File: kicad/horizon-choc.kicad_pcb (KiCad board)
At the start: 2 copper layers, 252.5 x 68 mm, 96 parts, among them J1 OLED, SW1 SW_Push, SW10 SW_Push, SW11 SW_Push, SW12 SW_Push, SW13 SW_Push, SW14 SW_Push, SW15 SW_Push, SW16 SW_Push, SW17 SW_Push, SW18 SW_Push, SW19 SW_Push, SW2 SW_Push, SW20 SW_Push, SW21 SW_Push, SW22 SW_Push, SW23 SW_Push, SW24 SW_Push, SW25 SW_Push, SW26 SW_Push, SW27 SW_Push, SW28 SW_Push, SW29 SW_Push, SW3 SW_Push, SW30 SW_Push, SW31 SW_Push, SW32 SW_Push, SW33 SW_Push, SW34 SW_Push, SW35 SW_Push, SW36 SW_Push, SW37 SW_Push, SW38 SW_Push, SW39 SW_Push, SW4 SW_Push, SW40 SW_Push, SW41 SW_Push, SW42 SW_Push, SW5 SW_Push, SW6 SW_Push, SW7 SW_Push, SW8 SW_Push, SW9 SW_Push, U1 PRO-MICRO

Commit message: Adjust center component layout for MX and Choc consistency.
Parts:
- moved D37 7.50 mm to (192.5, 141.5)
- moved D38 7.50 mm to (194.5, 141.5)
- moved D39 7.50 mm to (196.5, 141.5)
- moved D40 7.50 mm to (207.5, 141.5)
- moved D41 7.50 mm to (209.5, 141.5)
- moved D42 7.50 mm to (211.5, 141.5)
- moved TSW1 0.50 mm to (202.0, 141.5), turned to 90 degrees
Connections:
- D1 pad 1: (no net) -> ROW1
- D1 pad 2: (no net) -> Net-(D1-Pad2)
- D10 pad 1: (no net) -> ROW2
- D10 pad 2: (no net) -> Net-(D10-Pad2)
- D11 pad 1: (no net) -> ROW2
- D11 pad 2: (no net) -> Net-(D11-Pad2)
- D12 pad 1: (no net) -> ROW2
- D12 pad 2: (no net) -> Net-(D12-Pad2)
- D13 pad 1: (no net) -> ROW3
- D13 pad 2: (no net) -> Net-(D13-Pad2)
- D14 pad 1: (no net) -> ROW3
- D14 pad 2: (no net) -> Net-(D14-Pad2)
- D15 pad 1: (no net) -> ROW3
- D15 pad 2: (no net) -> Net-(D15-Pad2)
- D16 pad 1: (no net) -> ROW3
- D16 pad 2: (no net) -> Net-(D16-Pad2)
- D17 pad 1: (no net) -> ROW3
- D17 pad 2: (no net) -> Net-(D17-Pad2)
- D18 pad 1: (no net) -> ROW3
- D18 pad 2: (no net) -> Net-(D18-Pad2)
- D19 pad 1: (no net) -> ROW4
- D19 pad 2: (no net) -> Net-(D19-Pad2)
- D2 pad 1: (no net) -> ROW1
- D2 pad 2: (no net) -> Net-(D2-Pad2)
- D20 pad 1: (no net) -> ROW4
- D20 pad 2: (no net) -> Net-(D20-Pad2)
- D21 pad 1: (no net) -> ROW4
- D21 pad 2: (no net) -> Net-(D21-Pad2)
- D22 pad 1: (no net) -> ROW4
- D22 pad 2: (no net) -> Net-(D22-Pad2)
- D23 pad 1: (no net) -> ROW4
- D23 pad 2: (no net) -> Net-(D23-Pad2)
- D24 pad 1: (no net) -> ROW4
- D24 pad 2: (no net) -> Net-(D24-Pad2)
- D25 pad 1: (no net) -> ROW5
- D25 pad 2: (no net) -> Net-(D25-Pad2)
- D26 pad 1: (no net) -> ROW5
- D26 pad 2: (no net) -> Net-(D26-Pad2)
- D27 pad 1: (no net) -> ROW5
- D27 pad 2: (no net) -> Net-(D27-Pad2)
- D28 pad 1: (no net) -> ROW5
- D28 pad 2: (no net) -> Net-(D28-Pad2)
- D29 pad 1: (no net) -> ROW5
- D29 pad 2: (no net) -> Net-(D29-Pad2)
- D3 pad 1: (no net) -> ROW1
- D3 pad 2: (no net) -> Net-(D3-Pad2)
- D30 pad 1: (no net) -> ROW5
- D30 pad 2: (no net) -> Net-(D30-Pad2)
- D31 pad 1: (no net) -> ROW6
- D31 pad 2: (no net) -> Net-(D31-Pad2)
- D32 pad 1: (no net) -> ROW6
- D32 pad 2: (no net) -> Net-(D32-Pad2)
- D33 pad 1: (no net) -> ROW6
- D33 pad 2: (no net) -> Net-(D33-Pad2)
- D34 pad 1: (no net) -> ROW6
- D34 pad 2: (no net) -> Net-(D34-Pad2)
- D35 pad 1: (no net) -> ROW6
- D35 pad 2: (no net) -> Net-(D35-Pad2)
- D36 pad 1: (no net) -> ROW6
- D36 pad 2: (no net) -> Net-(D36-Pad2)
- D37 pad 1: (no net) -> ROW7
- D37 pad 2: (no net) -> Net-(D37-Pad2)
- D38 pad 1: (no net) -> ROW7
- D38 pad 2: (no net) -> Net-(D38-Pad2)
- D39 pad 1: (no net) -> ROW7
- D39 pad 2: (no net) -> Net-(D39-Pad2)
- D4 pad 1: (no net) -> ROW1
- D4 pad 2: (no net) -> Net-(D4-Pad2)
- D40 pad 1: (no net) -> ROW7
- D40 pad 2: (no net) -> Net-(D40-Pad2)
- D41 pad 1: (no net) -> ROW7
- D41 pad 2: (no net) -> Net-(D41-Pad2)
- D42 pad 1: (no net) -> ROW7
- D42 pad 2: (no net) -> Net-(D42-Pad2)
- D5 pad 1: (no net) -> ROW1
- D5 pad 2: (no net) -> Net-(D5-Pad2)
- D6 pad 1: (no net) -> ROW1
- D6 pad 2: (no net) -> Net-(D6-Pad2)
- D7 pad 1: (no net) -> ROW2
- D7 pad 2: (no net) -> Net-(D7-Pad2)
- D8 pad 1: (no net) -> ROW2
- D8 pad 2: (no net) -> Net-(D8-Pad2)
- D9 pad 1: (no net) -> ROW2
- D9 pad 2: (no net) -> Net-(D9-Pad2)
- H1 pad 1: (no net) -> Net-(H1-Pad1)
- H2 pad 1: (no net) -> Net-(H2-Pad1)
- H3 pad 1: (no net) -> Net-(H3-Pad1)
- H4 pad 1: (no net) -> Net-(H4-Pad1)
- J1 pad 1: (no net) -> GND
- J1 pad 2: (no net) -> VCC
- J1 pad 3: (no net) -> SCL
- J1 pad 4: (no net) -> SDA
- TSW1 pad 1: (no net) -> Net-(TSW1-Pad1)
- TSW1 pad 2: (no net) -> GND
- U1 pad 1: (no net) -> ROW2
- U1 pad 10: (no net) -> COL4
- U1 pad 11: (no net) -> COL5
- U1 pad 12: (no net) -> COL6
- U1 pad 13: (no net) -> ROW7
- U1 pad 14: (no net) -> ROW6
- U1 pad 15: (no net) -> ROW5
- U1 pad 16: (no net) -> ROW3
- U1 pad 17: (no net) -> ROW1
- U1 pad 2: (no net) -> ROW4
- U1 pad 21: (no net) -> VCC
- U1 pad 22: (no net) -> Net-(TSW1-Pad1)
- U1 pad 23: (no net) -> GND
- U1 pad 3: (no net) -> GND
- U1 pad 4: (no net) -> GND
- U1 pad 5: (no net) -> SDA
- U1 pad 6: (no net) -> SCL
- U1 pad 7: (no net) -> COL1
- U1 pad 8: (no net) -> COL2
- U1 pad 9: (no net) -> COL3

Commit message: Route traces on choc version
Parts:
- LOGO1: moved to F.Cu
- moved LOGO1 9.04 mm to (176.1, 174.7), turned to 0 degrees
- turned TSW1 to 0 degrees
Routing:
- net COL2: track 0.00 -> 317.8 mm
- net COL1: track 0.00 -> 317.3 mm
- net COL3: track 0.00 -> 312.2 mm
- net COL4: track 0.00 -> 308.4 mm
- net COL5: track 0.00 -> 306.0 mm
- net COL6: track 0.00 -> 304.9 mm
- net Net-(D12-Pad2): track 0.00 -> 115.5 mm
- net Net-(D36-Pad2): track 0.00 -> 113.4 mm
- net Net-(D24-Pad2): track 0.00 -> 112.4 mm
- net Net-(D1-Pad2): track 0.00 -> 104.4 mm
- net Net-(D25-Pad2): track 0.00 -> 101.9 mm
- net Net-(D13-Pad2): track 0.00 -> 101.0 mm
- net Net-(D35-Pad2): track 0.00 -> 96.5 mm
- net Net-(D11-Pad2): track 0.00 -> 95.9 mm
- net Net-(D23-Pad2): track 0.00 -> 94.5 mm
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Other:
- board size 252.5 x 68 mm -> 252 x 68 mm

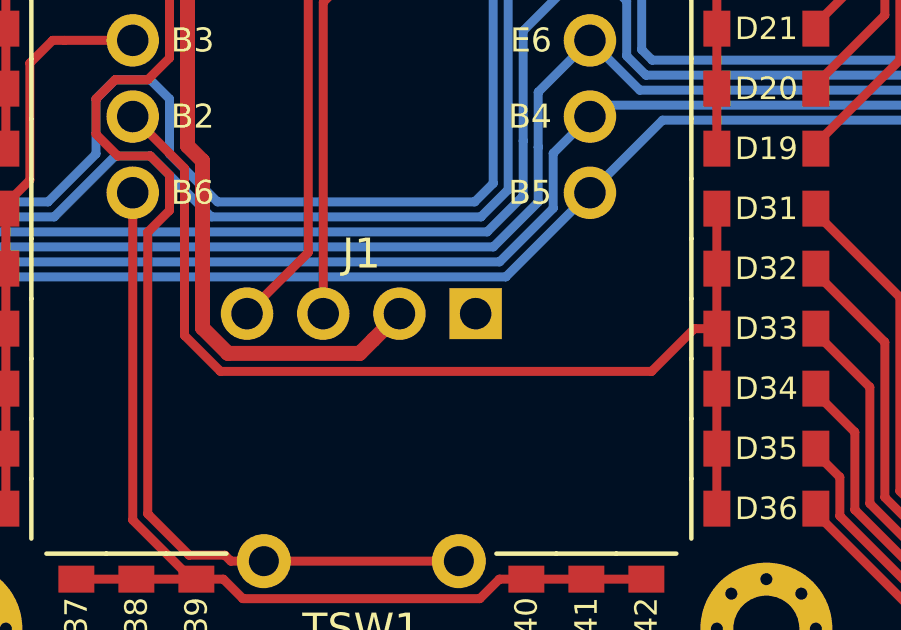
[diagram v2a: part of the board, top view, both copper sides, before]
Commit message: Route Choc board with diodes in center
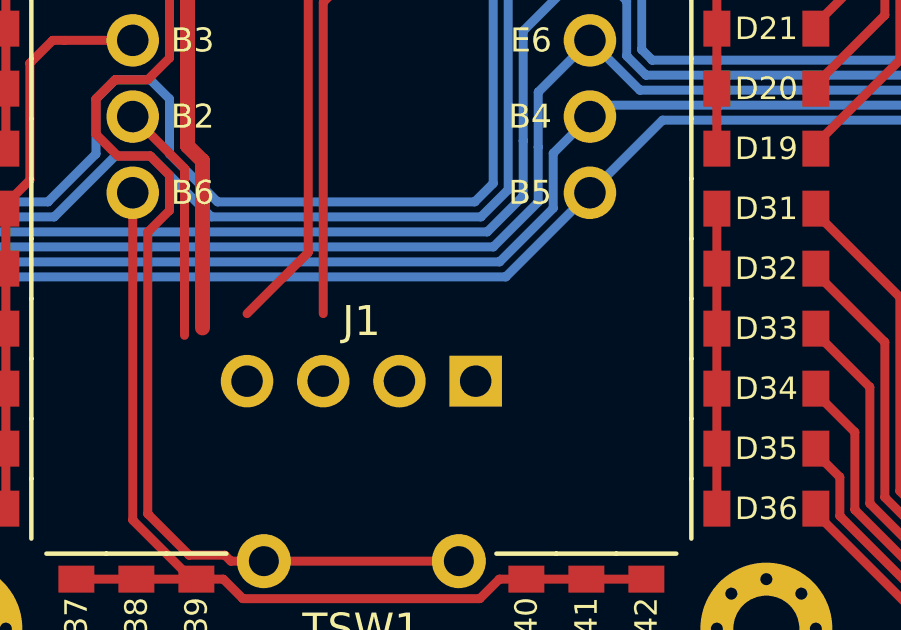
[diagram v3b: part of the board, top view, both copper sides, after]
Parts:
- moved J1 2.25 mm to (202.0, 133.2)
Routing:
- net ROW6: track 36.8 -> 18.0 mm
- net VCC: track 33.3 -> 25.9 mm

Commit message: Use 50 key layout on MX version
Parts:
- removed H5, H6, H7, H8: Hole_Pad, horizon-footprints:Mount_M2
- moved H2 30.0 mm to (245.5, 99.5)
- moved H4 30.0 mm to (245.5, 141.5)
- moved SW10 30.0 mm to (313.0, 103.5)
- moved SW11 30.0 mm to (331.0, 103.5)
- moved SW12 30.0 mm to (349.0, 103.5)
- moved SW19 30.0 mm to (259.0, 120.5)
- moved SW20 30.0 mm to (277.0, 120.5)
- moved SW21 30.0 mm to (295.0, 120.5)
- moved SW22 30.0 mm to (313.0, 120.5)
- moved SW23 30.0 mm to (331.0, 120.5)
- moved SW24 30.0 mm to (349.0, 120.5)
- moved SW31 30.0 mm to (259.0, 137.5)
- moved SW32 30.0 mm to (277.0, 137.5)
- moved SW33 30.0 mm to (295.0, 137.5)
- moved SW34 30.0 mm to (313.0, 137.5)
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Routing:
- net COL2: track 317.8 -> 0.00 mm
- net COL1: track 317.3 -> 0.00 mm
- net COL3: track 312.2 -> 0.00 mm
- net COL4: track 308.4 -> 0.00 mm
- net COL5: track 306.0 -> 0.00 mm
- net COL6: track 304.9 -> 0.00 mm
- net Net-(D12-Pad2): track 115.5 -> 0.00 mm
- net Net-(D36-Pad2): track 113.4 -> 0.00 mm
- net Net-(D24-Pad2): track 112.4 -> 0.00 mm
- net Net-(D1-Pad2): track 104.4 -> 0.00 mm
- net Net-(D25-Pad2): track 101.9 -> 0.00 mm
- net Net-(D13-Pad2): track 101.0 -> 0.00 mm
- net Net-(D35-Pad2): track 96.5 -> 0.00 mm
- net Net-(D11-Pad2): track 95.9 -> 0.00 mm
- net Net-(D23-Pad2): track 94.5 -> 0.00 mm
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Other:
- board size 252 x 68 mm -> 282 x 86.8 mm

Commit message: Implement battery on Choc version, plus bottom and top PCBs
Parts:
- removed the D25 at (202.5, 136.5)
- removed the D39 at (202.5, 142.5)
- removed J1: OLED, horizon-footprints:Header_1x04_2.54mm
- removed the SW25 at (85.0, 137.5)
- removed the SW39 at (204.0, 170.2)
- added D19: D, horizon-footprints:D_SOD-123, F.Cu at (229.0, 125.2)
- added D43: D, horizon-footprints:D_SOD-123, F.Cu at (157.0, 159.2)
- added D44: D, horizon-footprints:D_SOD-123, F.Cu at (175.0, 159.2)
- added D45: D, horizon-footprints:D_SOD-123, F.Cu at (193.0, 159.2)
- added D46: D, horizon-footprints:D_SOD-123, F.Cu at (211.0, 159.2)
- added D47: D, horizon-footprints:D_SOD-123, F.Cu at (229.0, 159.2)
- added D48: D, horizon-footprints:D_SOD-123, F.Cu at (247.0, 159.2)
- added D49: D, horizon-footprints:D_SOD-123, F.Cu at (265.0, 159.2)
- added D50: D, horizon-footprints:D_SOD-123, F.Cu at (283.0, 159.2)
- added D51: D, horizon-footprints:D_SOD-123, F.Cu at (301.0, 159.2)
- added D52: D, horizon-footprints:D_SOD-123, F.Cu at (319.0, 159.2)
- added D7: D, horizon-footprints:D_SOD-123, F.Cu at (229.0, 108.2)
- added H10: Hole_Pad, horizon-footprints:Mount_M2, F.Cu at (215.5, 99.5)
- added H11: Hole_Pad, horizon-footprints:Mount_M2, F.Cu at (188.5, 124.5)
- added H12: Hole_Pad, horizon-footprints:Mount_M2, F.Cu at (215.5, 124.5)
- added H5: Hole_Pad, horizon-footprints:Mount_M2, F.Cu at (94.0, 146.0)
- added H6: Hole_Pad, horizon-footprints:Mount_M2, F.Cu at (166.0, 146.0)
- added H7: Hole_Pad, horizon-footprints:Mount_M2, F.Cu at (238.0, 146.0)
- added H8: Hole_Pad, horizon-footprints:Mount_M2, F.Cu at (310.0, 146.0)
- added H9: Hole_Pad, horizon-footprints:Mount_M2, F.Cu at (188.5, 99.5)
- added SS1: POWER, horizon-footprints:SS12D00, F.Cu at (188.5, 112.0)
- added SW19: SW_Push, horizon-footprints:SW_Choc, F.Cu at (229.0, 120.5)
- added SW43: SW_Push, horizon-footprints:SW_Choc, F.Cu at (157.0, 154.5)
- added SW44: SW_Push, horizon-footprints:SW_Choc, F.Cu at (175.0, 154.5)
- added SW45: SW_Push, horizon-footprints:SW_Choc, F.Cu at (193.0, 154.5)
- added SW46: SW_Push, horizon-footprints:SW_Choc, F.Cu at (211.0, 154.5)
- added SW47: SW_Push, horizon-footprints:SW_Choc, F.Cu at (229.0, 154.5)
- added SW48: SW_Push, horizon-footprints:SW_Choc, F.Cu at (247.0, 154.5)
- added SW49: SW_Push, horizon-footprints:SW_Choc, F.Cu at (265.0, 154.5)
- added SW50: SW_Push, horizon-footprints:SW_Choc, F.Cu at (283.0, 154.5)
- added SW51: SW_Push, horizon-footprints:SW_Choc, F.Cu at (301.0, 154.5)
- added SW52: SW_Push, horizon-footprints:SW_Choc, F.Cu at (319.0, 154.5)
- added SW7: SW_Push, horizon-footprints:SW_Choc, F.Cu at (229.0, 103.5)
- added W1: BATTERY, horizon-footprints:Battery_Wire_Pads, F.Cu at (188.5, 106.2)
- LOGO1: moved to B.Cu
- moved SW39 177.3 mm to (85.0, 154.5)
- moved SW13 174.8 mm to (85.0, 120.5)
- moved D39 153.1 mm to (85.0, 159.2)
- moved D13 150.8 mm to (85.0, 125.2)
- moved SW37 136.1 mm to (301.0, 137.5)
- moved SW38 134.1 mm to (319.0, 137.5), turned to 0 degrees
- moved D40 132.1 mm to (103.0, 159.2)
- moved SW42 129.0 mm to (139.0, 154.5)
- moved SW40 128.0 mm to (103.0, 154.5), turned to 0 degrees
- moved SW41 126.5 mm to (121.0, 154.5), turned to 0 degrees
- moved D25 120.7 mm to (85.0, 142.2), turned to 0 degrees
- moved D1 117.6 mm to (85.0, 108.2), turned to 0 degrees
- moved D38 116.5 mm to (319.0, 142.2), turned to 0 degrees
- moved D41 114.6 mm to (121.0, 159.2)
- moved D14 99.9 mm to (103.0, 125.2), turned to 0 degrees
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- renumbered TSW1 to BTN1, D7 to D13, D13 to D25, D19 to D39, SW7 to SW13, SW13 to SW25, SW19 to SW39
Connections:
- net Net-(TSW1-Pad1) renamed RESET
- D10 pad 1: ROW2 -> ROW1
- D11 pad 1: ROW2 -> ROW1
- D12 pad 1: ROW2 -> ROW1
- D14 pad 1: ROW3 -> ROW2
- D15 pad 1: ROW3 -> ROW2
- D16 pad 1: ROW3 -> ROW2
- D17 pad 1: ROW3 -> ROW2
- D18 pad 1: ROW3 -> ROW2
- D20 pad 1: ROW4 -> ROW2
- D21 pad 1: ROW4 -> ROW2
- D22 pad 1: ROW4 -> ROW2
- D23 pad 1: ROW4 -> ROW2
- D24 pad 1: ROW4 -> ROW2
- D26 pad 1: ROW5 -> ROW3
- D27 pad 1: ROW5 -> ROW3
- D28 pad 1: ROW5 -> ROW3
- D29 pad 1: ROW5 -> ROW3
- D30 pad 1: ROW5 -> ROW3
- D31 pad 1: ROW6 -> ROW3
- D32 pad 1: ROW6 -> ROW3
- D33 pad 1: ROW6 -> ROW3
- D34 pad 1: ROW6 -> ROW3
- D35 pad 1: ROW6 -> ROW3
- D36 pad 1: ROW6 -> ROW3
- D37 pad 1: ROW7 -> ROW3
- D38 pad 1: ROW7 -> ROW3
- D40 pad 1: ROW7 -> ROW4
- D41 pad 1: ROW7 -> ROW4
- D42 pad 1: ROW7 -> ROW4
- D8 pad 1: ROW2 -> ROW1
- D9 pad 1: ROW2 -> ROW1
- SW10 pad 1: COL4 -> COL12
- SW11 pad 1: COL5 -> COL13
- SW12 pad 1: COL6 -> COL14
- SW20 pad 1: COL2 -> COL10
- SW21 pad 1: COL3 -> COL11
- SW22 pad 1: COL4 -> COL12
- SW23 pad 1: COL5 -> COL13
- SW24 pad 1: COL6 -> COL14
- SW31 pad 1: COL1 -> COL7
- SW32 pad 1: COL2 -> COL8
- SW33 pad 1: COL3 -> COL9
- SW34 pad 1: COL4 -> COL10
- SW35 pad 1: COL5 -> COL11
- SW36 pad 1: COL6 -> COL12
- SW37 pad 1: COL1 -> COL13
- SW38 pad 1: COL2 -> COL14
- SW40 pad 1: COL4 -> COL2
- SW41 pad 1: COL5 -> COL3
- SW42 pad 1: COL6 -> COL4
- SW8 pad 1: COL2 -> COL10
- SW9 pad 1: COL3 -> COL11
- U1 pad 1: ROW2 -> ROW1
- U1 pad 10: COL4 -> COL9
- U1 pad 11: COL5 -> COL8
- U1 pad 12: COL6 -> ROW4
- U1 pad 13: ROW7 -> ROW3
- U1 pad 14: ROW6 -> COL7
- U1 pad 15: ROW5 -> COL6
- U1 pad 16: ROW3 -> COL5
- U1 pad 17: ROW1 -> COL4
- U1 pad 18: (no net) -> COL3
- U1 pad 19: (no net) -> COL2
- U1 pad 2: ROW4 -> ROW2
- U1 pad 20: (no net) -> COL1
- U1 pad 21: VCC -> (no net)
- U1 pad 24: (no net) -> RAW
- U1 pad 5: SDA -> COL14
- U1 pad 6: SCL -> COL13
- U1 pad 7: COL1 -> COL12
- U1 pad 8: COL2 -> COL11
- U1 pad 9: COL3 -> COL10
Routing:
- net ROW4: track 0.00 -> 295.8 mm, vias 0 -> 1
- net ROW2: track 0.00 -> 287.1 mm
- net ROW3: track 0.00 -> 278.8 mm, vias 0 -> 1
- net ROW1: track 0.00 -> 264.1 mm
- net COL1: track 0.00 -> 184.9 mm
- net COL14: track 0.00 -> 184.9 mm
- net COL2: track 0.00 -> 164.8 mm
- net COL13: track 0.00 -> 164.8 mm
- net COL3: track 0.00 -> 144.7 mm
- net COL12: track 0.00 -> 144.7 mm
- net COL4: track 0.00 -> 124.6 mm
- net COL11: track 0.00 -> 124.6 mm
- net COL5: track 0.00 -> 105.8 mm
- net COL10: track 0.00 -> 105.2 mm
- net COL9: track 0.00 -> 86.1 mm
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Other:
- board size 282 x 86.8 mm -> 252 x 68 mm
- board text added: "RESET"

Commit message: Use 50-key layout
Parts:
- removed the D31 at (193.0, 142.2)
- removed the D32 at (211.0, 142.2)
- removed H10, H11, H12, H9: Hole_Pad, horizon-footprints:Mount_M2
- removed the SW31 at (193.0, 137.5)
- removed the SW32 at (211.0, 137.5)
- moved H3 148.0 mm to (94.0, 146.0)
- moved H2 144.0 mm to (310.0, 112.0)
- moved H5 105.3 mm to (188.5, 99.5)
- moved H8 94.6 mm to (215.5, 141.5)
- moved H6 67.9 mm to (215.5, 99.5)
- moved H7 49.7 mm to (188.5, 141.5)
- moved W1 37.9 mm to (202.2, 141.5), turned to 180 degrees
- moved H4 34.0 mm to (310.0, 146.0)
- moved LOGO1 27.6 mm to (201.5, 170.5)
- moved BTN1 23.2 mm to (209.6, 134.0), turned to 0 degrees
- moved SS1 22.7 mm to (194.4, 134.0), turned to 180 degrees
- renumbered D33 to D31, D34 to D32, D35 to D33, D36 to D34, D37 to D35, D38 to D36, D39 to D37, D40 to D38, D41 to D39, D42 to D40, D43 to D41, D44 to D42, D45 to D43, D46 to D44, D47 to D45, D48 to D46, D49 to D47, D50 to D48, D51 to D49, D52 to D50, SW33 to SW31, SW34 to SW32, SW35 to SW33, SW36 to SW34, SW37 to SW35, SW38 to SW36, SW39 to SW37, SW40 to SW38, SW41 to SW39, SW42 to SW40, SW43 to SW41, SW44 to SW42, SW45 to SW43, SW46 to SW44, SW47 to SW45, SW48 to SW46, SW49 to SW47, SW50 to SW48, SW51 to SW49, SW52 to SW50
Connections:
- U1 pad 10: COL9 -> COL10
- U1 pad 11: COL8 -> COL9
- U1 pad 12: ROW4 -> COL8
- U1 pad 13: ROW3 -> COL7
- U1 pad 14: COL7 -> COL6
- U1 pad 15: COL6 -> COL5
- U1 pad 16: COL5 -> COL4
- U1 pad 17: COL4 -> COL3
- U1 pad 18: COL3 -> COL2
- U1 pad 19: COL2 -> COL1
- U1 pad 20: COL1 -> ROW4
- U1 pad 5: COL14 -> ROW3
- U1 pad 6: COL13 -> COL14
- U1 pad 7: COL12 -> COL13
- U1 pad 8: COL11 -> COL12
- U1 pad 9: COL10 -> COL11
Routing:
- net RAW: track 13.6 -> 37.1 mm
- net ROW4: track 295.8 -> 314.6 mm, vias 1 -> 0
- net ROW3: track 278.8 -> 295.5 mm, vias 1 -> 3
- net RESET: track 27.1 -> 39.1 mm
- net Net-(D32-Pad2) (its old number): track 9.89 -> 0.00 mm
- net Net-(D31-Pad2) (its old number): track 9.89 -> 0.00 mm
- net ROW2: track 287.1 -> 296.0 mm
- net COL8: track 27.4 -> 22.2 mm
- net COL7: track 27.4 -> 22.2 mm
- net +BATT: track 6.77 -> 10.3 mm
- net COL9: track 86.1 -> 85.1 mm
- net COL6: track 86.1 -> 85.1 mm
- net COL11: track 124.6 -> 125.3 mm
- net COL4: track 124.6 -> 125.3 mm
- net COL14: track 184.9 -> 185.7 mm
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
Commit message: Layout MX PCB
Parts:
- added D31: D, horizon-footprints:D_SOD-123, B.Cu at (193.0, 142.2)
- added D32: D, horizon-footprints:D_SOD-123, B.Cu at (211.0, 142.2)
- added SW31: SW_Push, horizon-footprints:SW_Choc, F.Cu at (193.0, 137.5)
- added SW32: SW_Push, horizon-footprints:SW_Choc, F.Cu at (211.0, 137.5)
- D1, D10, D11, D12, D13, D14, D15, D16, D17, D18, D19, D2, D20, D21, D22, D23, D24, D25, D26, D27, D28, D29, D3, D30, D4, D5, D6, D7, D8, D9: moved to B.Cu
- D33: renamed from D31; moved to B.Cu
- D34: renamed from D32; moved to B.Cu
- D35: renamed from D33; moved to B.Cu
- D36: renamed from D34; moved to B.Cu
- D37: renamed from D35; moved to B.Cu
- D38: renamed from D36; moved to B.Cu
- D39: renamed from D37; moved to B.Cu
- D40: renamed from D38; moved to B.Cu
- D41: renamed from D39; moved to B.Cu
- D42: renamed from D40; moved to B.Cu
- D43: renamed from D41; moved to B.Cu
- D44: renamed from D42; moved to B.Cu
- D45: renamed from D43; moved to B.Cu
- D46: renamed from D44; moved to B.Cu
- D47: renamed from D45; moved to B.Cu
- D48: renamed from D46; moved to B.Cu
- D49: renamed from D47; moved to B.Cu
- D50: renamed from D48; moved to B.Cu
- D51: renamed from D49; moved to B.Cu
- D52: renamed from D50; moved to B.Cu
- LOGO1: footprint horizon-footprints:Logo_Horizon -> horizon-footprints:Logo_Horizon_Small
- TB1: renamed from W1; footprint horizon-footprints:Battery_Wire_Pads -> horizon-footprints:KF350-2P
- moved LOGO1 47.0 mm to (202.0, 123.5)
- moved TB1 32.3 mm to (215.5, 112.0), turned to 0 degrees
- moved BTN1 28.4 mm to (188.5, 115.0), turned to 270 degrees
- moved SS1 26.6 mm to (188.5, 108.0), turned to 0 degrees
- moved H7 17.0 mm to (188.5, 124.5)
- moved H8 17.0 mm to (215.5, 124.5)
- renumbered SW31 to SW33, SW32 to SW34, SW33 to SW35, SW34 to SW36, SW35 to SW37, SW36 to SW38, SW37 to SW39, SW38 to SW40, SW39 to SW41, SW40 to SW42, SW41 to SW43, SW42 to SW44, SW43 to SW45, SW44 to SW46, SW45 to SW47, SW46 to SW48, SW47 to SW49, SW48 to SW50, SW49 to SW51, SW50 to SW52
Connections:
- SS1 pad 1: RAW -> (no net)
- SS1 pad 3: (no net) -> RAW
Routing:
- net +BATT: track 10.3 -> 46.6 mm
- net RAW: track 37.1 -> 10.4 mm
- net RESET: track 39.1 -> 15.6 mm
- net ROW2: track 296.0 -> 284.4 mm
- net Net-(D32-Pad2): track 0.00 -> 9.89 mm
- net Net-(D31-Pad2): track 0.00 -> 9.89 mm
- net COL8: track 22.2 -> 24.9 mm
- net COL7: track 22.2 -> 24.9 mm
- net COL14: track 185.7 -> 183.5 mm
- net COL4: track 125.3 -> 123.2 mm
- net COL11: track 125.3 -> 123.2 mm
- net COL2: track 165.6 -> 163.4 mm
- net COL13: track 165.6 -> 163.4 mm
- net COL12: track 145.4 -> 143.3 mm
- net COL1: track 185.7 -> 183.5 mm
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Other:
- board text added: "BATTERY"
- board text added: "OFF"
- board text added: "ON"
- board text added: "rev2 | Choc"
- board text removed: "rev2"
